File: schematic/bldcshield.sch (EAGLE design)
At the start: 39 parts, among them IC1 IR2101SMD, IC2 IR2101SMD, IC3 IR2101SMD, Q1 MOSFET-NCHANNELPTH2, Q2 MOSFET-NCHANNELPTH2, Q3 Shield, Q4 MOSFET-NCHANNELPTH2, Q5 MOSFET-NCHANNELPTH2, Q6 MOSFET-NCHANNELPTH2, Q7 MOSFET-NCHANNELPTH2, U3 LM317DCY, X1 MKDSN1,5/2-5,08, X2 MKDSN1,5/3-5,08

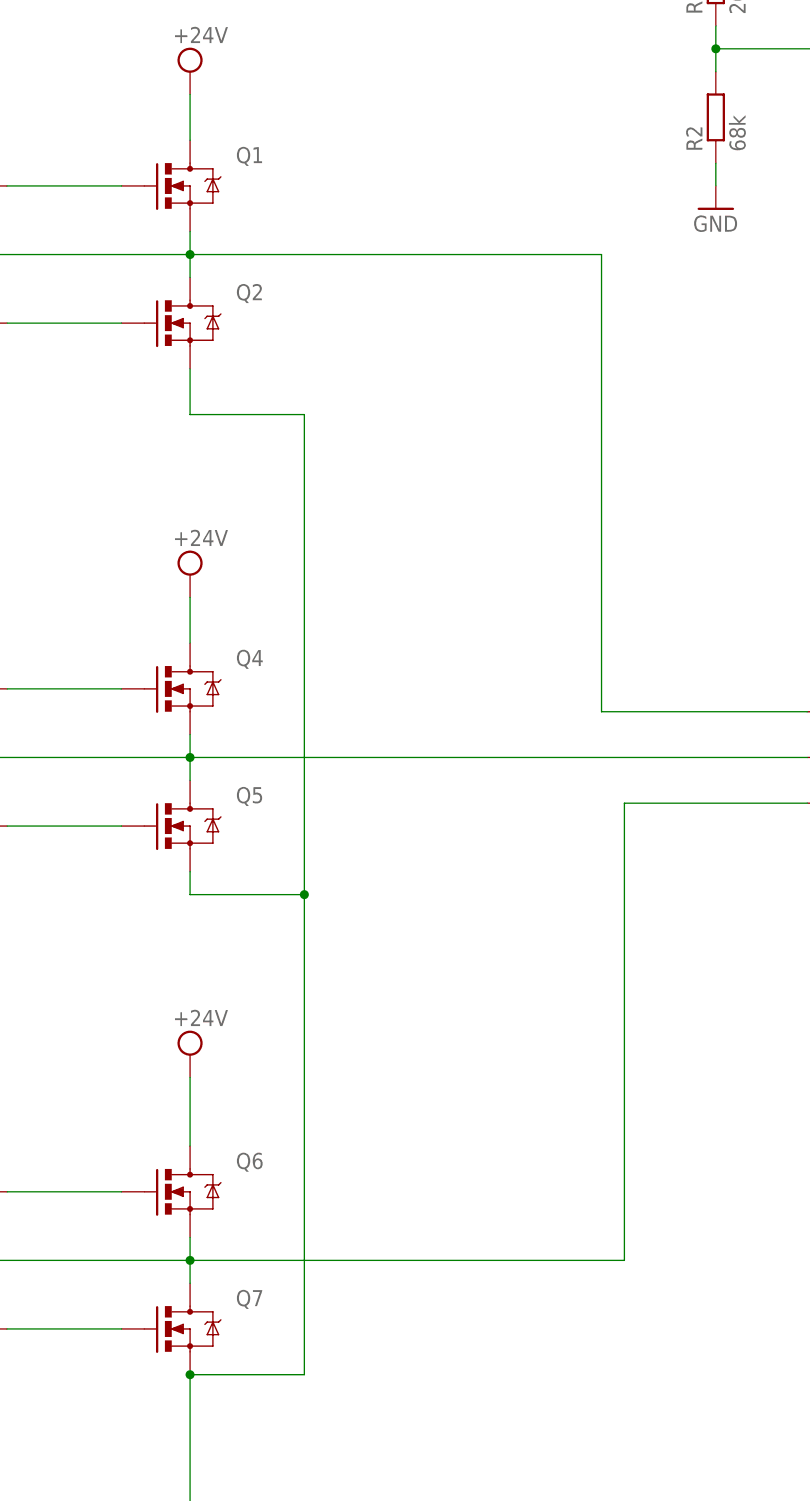
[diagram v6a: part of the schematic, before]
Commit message: changed to d-paks on both sides of the board, working on traces. moved to eagle 7.6
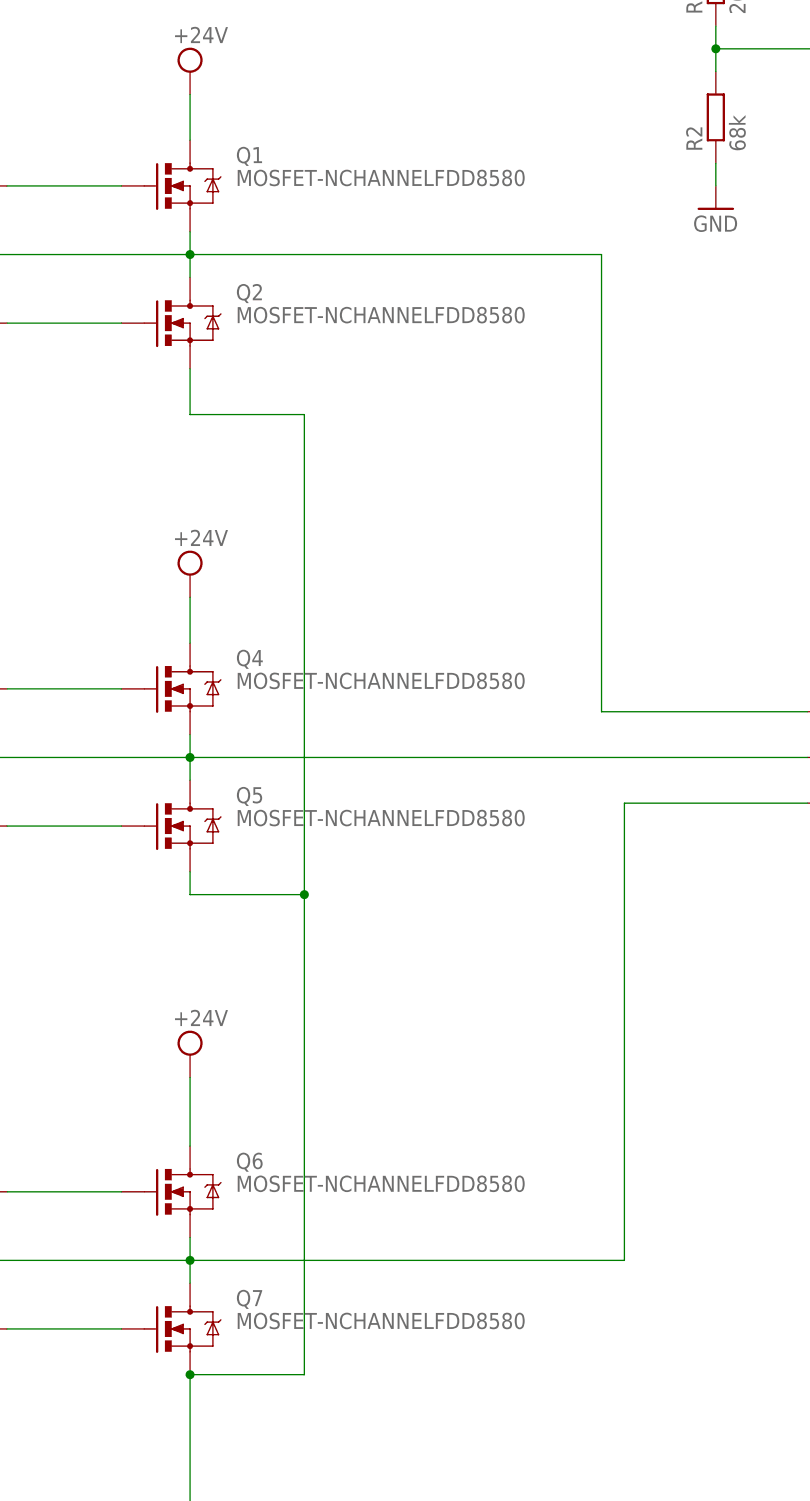
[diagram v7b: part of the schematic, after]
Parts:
- Q1, Q2, Q4, Q5, Q6, Q7: value MOSFET-NCHANNELPTH2 -> MOSFET-NCHANNELFDD8580; device SparkFun:MOSFET-NCHANNELPTH2 -> SparkFun:MOSFET-NCHANNELFDD8580
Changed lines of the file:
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@@
 <?xml version="1.0" encoding="utf-8"?>
 <!DOCTYPE eagle SYSTEM "eagle.dtd">
-<eagle version="6.5.0">
+<eagle version="7.6.0">
 <drawing>
 <settings>
@@
 <grid distance="0.1" unitdist="inch" unit="inch" style="lines" multiple="1" display="no" altdistance="0.01" altunitdist="inch" altunit="inch"/>
 <layers>
-<layer number="1" name="Top" color="4" fill="1" visible="no" active="no"/>
-<layer number="2" name="Route2" color="1" fill="3" visible="no" active="no"/>
-<layer number="3" name="Route3" color="4" fill="3" visible="no" active="no"/>
-<layer number="4" name="Route4" color="1" fill="4" visible="no" active="no"/>
-<layer number="5" name="Route5" color="4" fill="4" visible="no" active="no"/>
-<layer number="6" name="Route6" color="1" fill="8" visible="no" active="no"/>
-<layer number="7" name="Route7" color="4" fill="8" visible="no" active="no"/>
-<layer number="8" name="Route8" color="1" fill="2" visible="no" active="no"/>
-<layer number="9" name="Route9" color="4" fill="2" visible="no" active="no"/>
-<layer number="10" name="Route10" color="1" fill="7" visible="no" active="no"/>
-<layer number="11" name="Route11" color="4" fill="7" visible="no" active="no"/>
-<layer number="12" name="Route12" color="1" fill="5" visible="no" active="no"/>
-<layer number="13" name="Route13" color="4" fill="5" visible="no" active="no"/>
-<layer number="14" name="Route14" color="1" fill="6" visible="no" active="no"/>
-<layer number="15" name="Route15" color="4" fill="6" visible="no" active="no"/>
-<layer number="16" name="Bottom" color="1" fill="1" visible="no" active="no"/>
-<layer number="17" name="Pads" color="2" fill="1" visible="no" active="no"/>
-<layer number="18" name="Vias" color="14" fill="1" visible="no" active="no"/>
-<layer number="19" name="Unrouted" color="6" fill="1" visible="no" active="no"/>
-<layer number="20" name="Dimension" color="15" fill="1" visible="no" active="no"/>
-<layer number="21" name="tPlace" color="7" fill="1" visible="no" active="no"/>
-<layer number="22" name="bPlace" color="7" fill="1" visible="no" active="no"/>
-<layer number="23" name="tOrigins" color="15" fill="1" visible="no" active="no"/>
-<layer number="24" name="bOrigins" color="15" fill="1" visible="no" active="no"/>
-<layer number="25" name="tNames" color="7" fill="1" visible="no" active="no"/>
-<layer number="26" name="bNames" color="7" fill="1" visible="no" active="no"/>
-<layer number="27" name="tValues" color="7" fill="1" visible="no" active="no"/>
-<layer number="28" name="bValues" color="7" fill="1" visible="no" active="no"/>
-<layer number="29" name="tStop" color="2" fill="3" visible="no" active="no"/>
-<layer number="30" name="bStop" color="5" fill="6" visible="no" active="no"/>
+<layer number="1" name="Top" color="4" fill="1" visible="yes" active="no"/>
+<layer number="2" name="Route2" color="1" fill="3" visible="yes" active="no"/>
+<layer number="3" name="Route3" color="4" fill="3" visible="yes" active="no"/>
+<layer number="4" name="Route4" color="1" fill="4" visible="yes" active="no"/>
+<layer number="5" name="Route5" color="4" fill="4" visible="yes" active="no"/>
+<layer number="6" name="Route6" color="1" fill="8" visible="yes" active="no"/>
+<layer number="7" name="Route7" color="4" fill="8" visible="yes" active="no"/>
+<layer number="8" name="Route8" color="1" fill="2" visible="yes" active="no"/>
+<layer number="9" name="Route9" color="4" fill="2" visible="yes" active="no"/>
+<layer number="10" name="Route10" color="1" fill="7" visible="yes" active="no"/>
+<layer number="11" name="Route11" color="4" fill="7" visible="yes" active="no"/>
+<layer number="12" name="Route12" color="1" fill="5" visible="yes" active="no"/>
+<layer number="13" name="Route13" color="4" fill="5" visible="yes" active="no"/>
+<layer number="14" name="Route14" color="1" fill="6" visible="yes" active="no"/>
+<layer number="15" name="Route15" color="4" fill="6" visible="yes" active="no"/>
+<layer number="16" name="Bottom" color="1" fill="1" visible="yes" active="no"/>
+<layer number="17" name="Pads" color="2" fill="1" visible="yes" active="no"/>
+<layer number="18" name="Vias" color="2" fill="1" visible="yes" active="no"/>
+<layer number="19" name="Unrouted" color="6" fill="1" visible="yes" active="no"/>
+<layer number="20" name="Dimension" color="15" fill="1" visible="yes" active="no"/>
+<layer number="21" name="tPlace" color="7" fill="1" visible="yes" active="no"/>
+<layer number="22" name="bPlace" color="7" fill="1" visible="yes" active="no"/>
+<layer number="23" name="tOrigins" color="15" fill="1" visible="yes" active="no"/>
+<layer number="24" name="bOrigins" color="15" fill="1" visible="yes" active="no"/>
+<layer number="25" name="tNames" color="7" fill="1" visible="yes" active="no"/>
+<layer number="26" name="bNames" color="7" fill="1" visible="yes" active="no"/>
+<layer number="27" name="tValues" color="7" fill="1" visible="yes" active="no"/>
+<layer number="28" name="bValues" color="7" fill="1" visible="yes" active="no"/>
+<layer number="29" name="tStop" color="7" fill="3" visible="no" active="no"/>
+<layer number="30" name="bStop" color="7" fill="6" visible="no" active="no"/>
 <layer number="31" name="tCream" color="7" fill="4" visible="no" active="no"/>
 <layer number="32" name="bCream" color="7" fill="5" visible="no" active="no"/>
@@
 <layer number="35" name="tGlue" color="7" fill="4" visible="no" active="no"/>
 <layer number="36" name="bGlue" color="7" fill="5" visible="no" active="no"/>
-<layer number="37" name="tTest" color="7" fill="1" visible="no" active="no"/>
-<layer number="38" name="bTest" color="7" fill="1" visible="no" active="no"/>
+<layer number="37" name="tTest" color="7" fill="1" visible="yes" active="no"/>
+<layer number="38" name="bTest" color="7" fill="1" visible="yes" active="no"/>
 <layer number="39" name="tKeepout" color="4" fill="11" visible="no" active="no"/>
 <layer number="40" name="bKeepout" color="1" fill="11" visible="no" active="no"/>
@@
 <layer number="44" name="Drills" color="7" fill="1" visible="no" active="no"/>
 <layer number="45" name="Holes" color="7" fill="1" visible="no" active="no"/>
-<layer number="46" name="Milling" color="3" fill="1" visible="no" active="no"/>
-<layer number="47" name="Measures" color="7" fill="1" visible="no" active="no"/>
-<layer number="48" name="Document" color="7" fill="1" visible="no" active="no"/>
-<layer number="49" name="Reference" color="13" fill="1" visible="no" active="no"/>
-<layer number="50" name="dxf" color="12" fill="1" visible="no" active="no"/>
-<layer number="51" name="tDocu" color="7" fill="1" visible="no" active="no"/>
-<layer number="52" name="bDocu" color="7" fill="1" visible="no" active="no"/>
-<layer number="53" name="tGND_GNDA" color="7" fill="1" visible="no" active="no"/>
-<layer number="54" name="bGND_GNDA" color="7" fill="1" visible="no" active="no"/>
-<layer number="56" name="wert" color="7" fill="1" visible="no" active="no"/>
-<layer number="57" name="tCAD" color="7" fill="1" visible="no" active="no"/>
+<layer number="46" name="Milling" color="3" fill="1" visible="yes" active="no"/>
+<layer number="47" name="Measures" color="7" fill="1" visible="yes" active="no"/>
+<layer number="48" name="Document" color="7" fill="1" visible="yes" active="no"/>
+<layer number="49" name="Reference" color="7" fill="1" visible="yes" active="no"/>
+<layer number="50" name="dxf" color="12" fill="1" visible="yes" active="no"/>
+<layer number="51" name="tDocu" color="7" fill="1" visible="yes" active="no"/>
+<layer number="52" name="bDocu" color="7" fill="1" visible="yes" active="no"/>
+<layer number="53" name="tGND_GNDA" color="7" fill="1" visible="yes" active="no"/>
+<layer number="54" name="bGND_GNDA" color="7" fill="1" visible="yes" active="no"/>
+<layer number="56" name="wert" color="7" fill="1" visible="yes" active="no"/>
+<layer number="57" name="tCAD" color="7" fill="1" visible="yes" active="no"/>
 <layer number="90" name="Modules" color="5" fill="1" visible="yes" active="yes"/>
 <layer number="91" name="Nets" color="2" fill="1" visible="yes" active="yes"/>
@@
 </classes>
 <parts>
-<part name="Q1" library="SparkFun" deviceset="MOSFET-NCHANNEL" device="PTH2" value=""/>
-<part name="Q2" library="SparkFun" deviceset="MOSFET-NCHANNEL" device="PTH2" value=""/>
-<part name="Q4" library="SparkFun" deviceset="MOSFET-NCHANNEL" device="PTH2" value=""/>
-<part name="Q5" library="SparkFun" deviceset="MOSFET-NCHANNEL" device="PTH2" value=""/>
-<part name="Q6" library="SparkFun" deviceset="MOSFET-NCHANNEL" device="PTH2" value=""/>
-<part name="Q7" library="SparkFun" deviceset="MOSFET-NCHANNEL" device="PTH2" value=""/>
+<part name="Q1" library="SparkFun" deviceset="MOSFET-NCHANNEL" device="FDD8580" value="MOSFET-NCHANNELFDD8580"/>
+<part name="Q2" library="SparkFun" deviceset="MOSFET-NCHANNEL" device="FDD8580" value="MOSFET-NCHANNELFDD8580"/>
+<part name="Q4" library="SparkFun" deviceset="MOSFET-NCHANNEL" device="FDD8580" value="MOSFET-NCHANNELFDD8580"/>
+<part name="Q5" library="SparkFun" deviceset="MOSFET-NCHANNEL" device="FDD8580" value="MOSFET-NCHANNELFDD8580"/>
+<part name="Q6" library="SparkFun" deviceset="MOSFET-NCHANNEL" device="FDD8580" value="MOSFET-NCHANNELFDD8580"/>
+<part name="Q7" library="SparkFun" deviceset="MOSFET-NCHANNEL" device="FDD8580" value="MOSFET-NCHANNELFDD8580"/>
 <part name="R27" library="SmartPrj" deviceset="R-EU_" device="R1206" value="4.7k"/>
 <part name="C8" library="SmartPrj" deviceset="C-EU" device="C1206" value="22p"/>
